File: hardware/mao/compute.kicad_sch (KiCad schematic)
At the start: 49 parts, among them J201 TAG, U201 ESP32-S3-MINI-1-N8

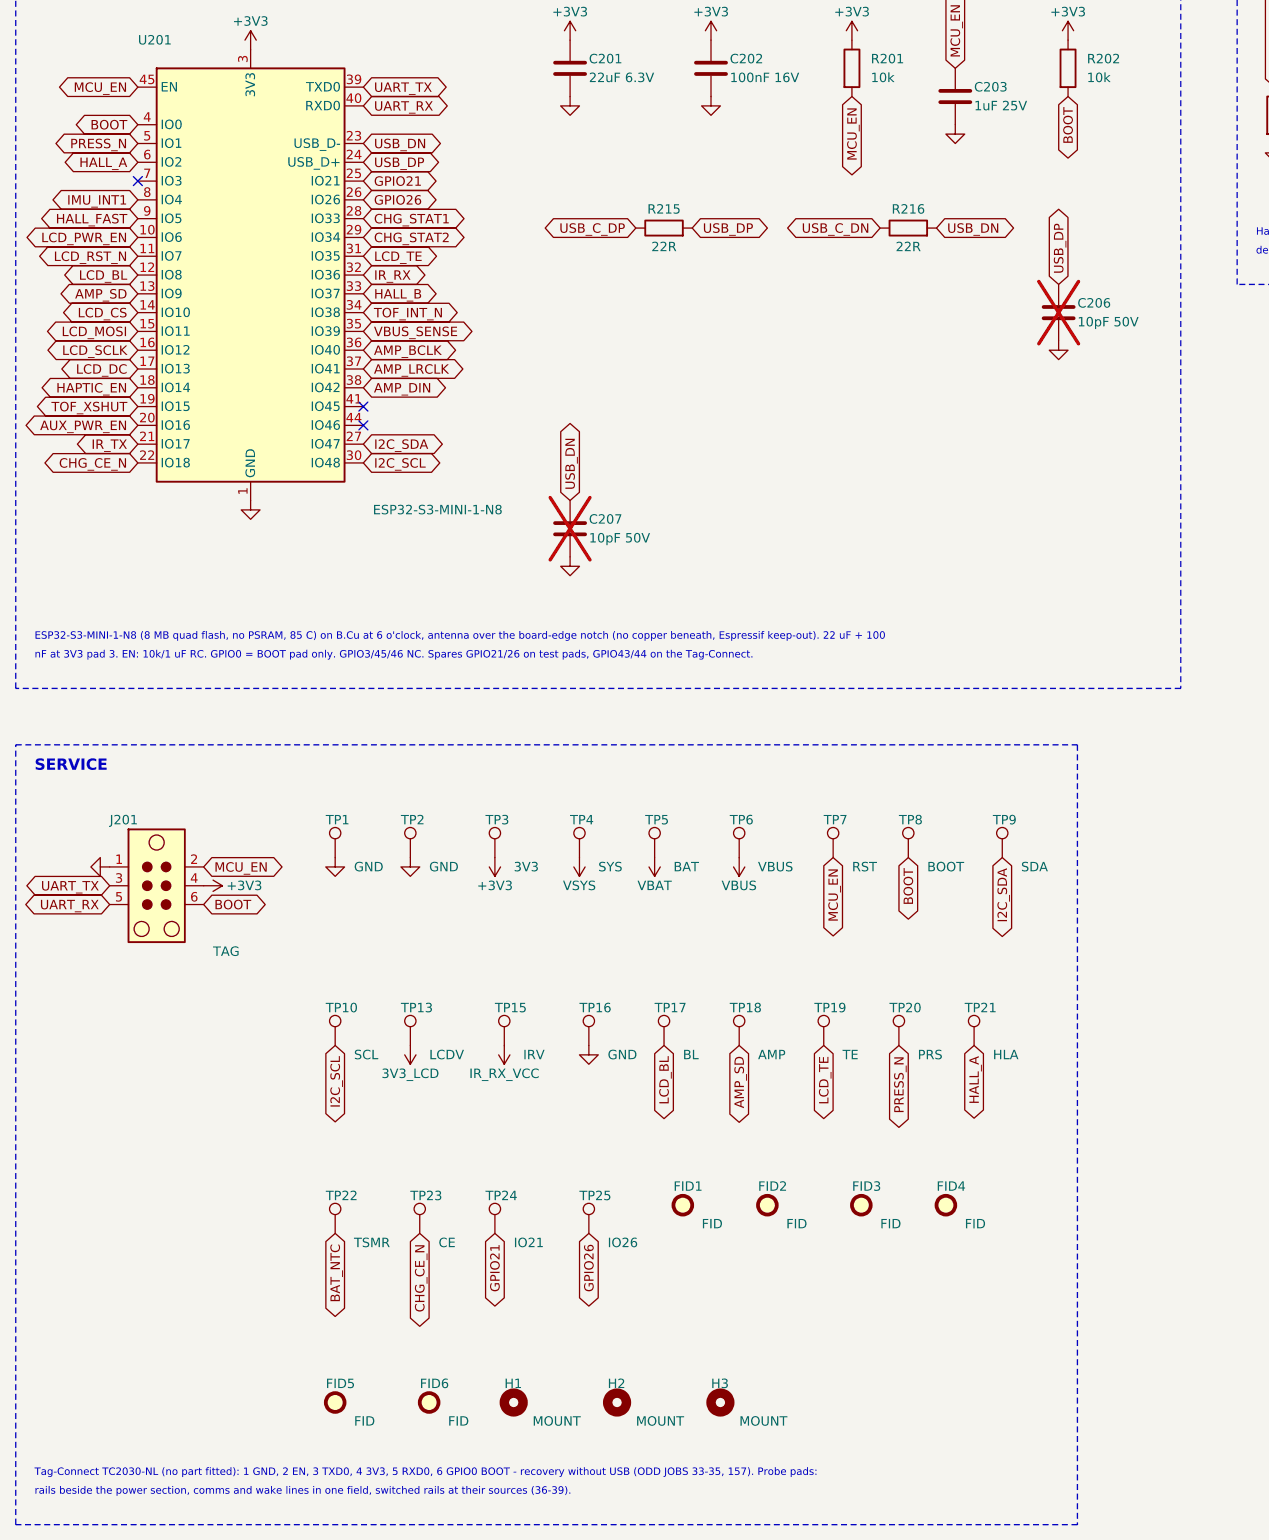
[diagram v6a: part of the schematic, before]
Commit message: A1 capture/layout follow the pin swaps (ERC 0); escapes and fixture pads moved with their nets
Co-Authored-By: Claude Opus 5.5 <noreply@anthropic.com>
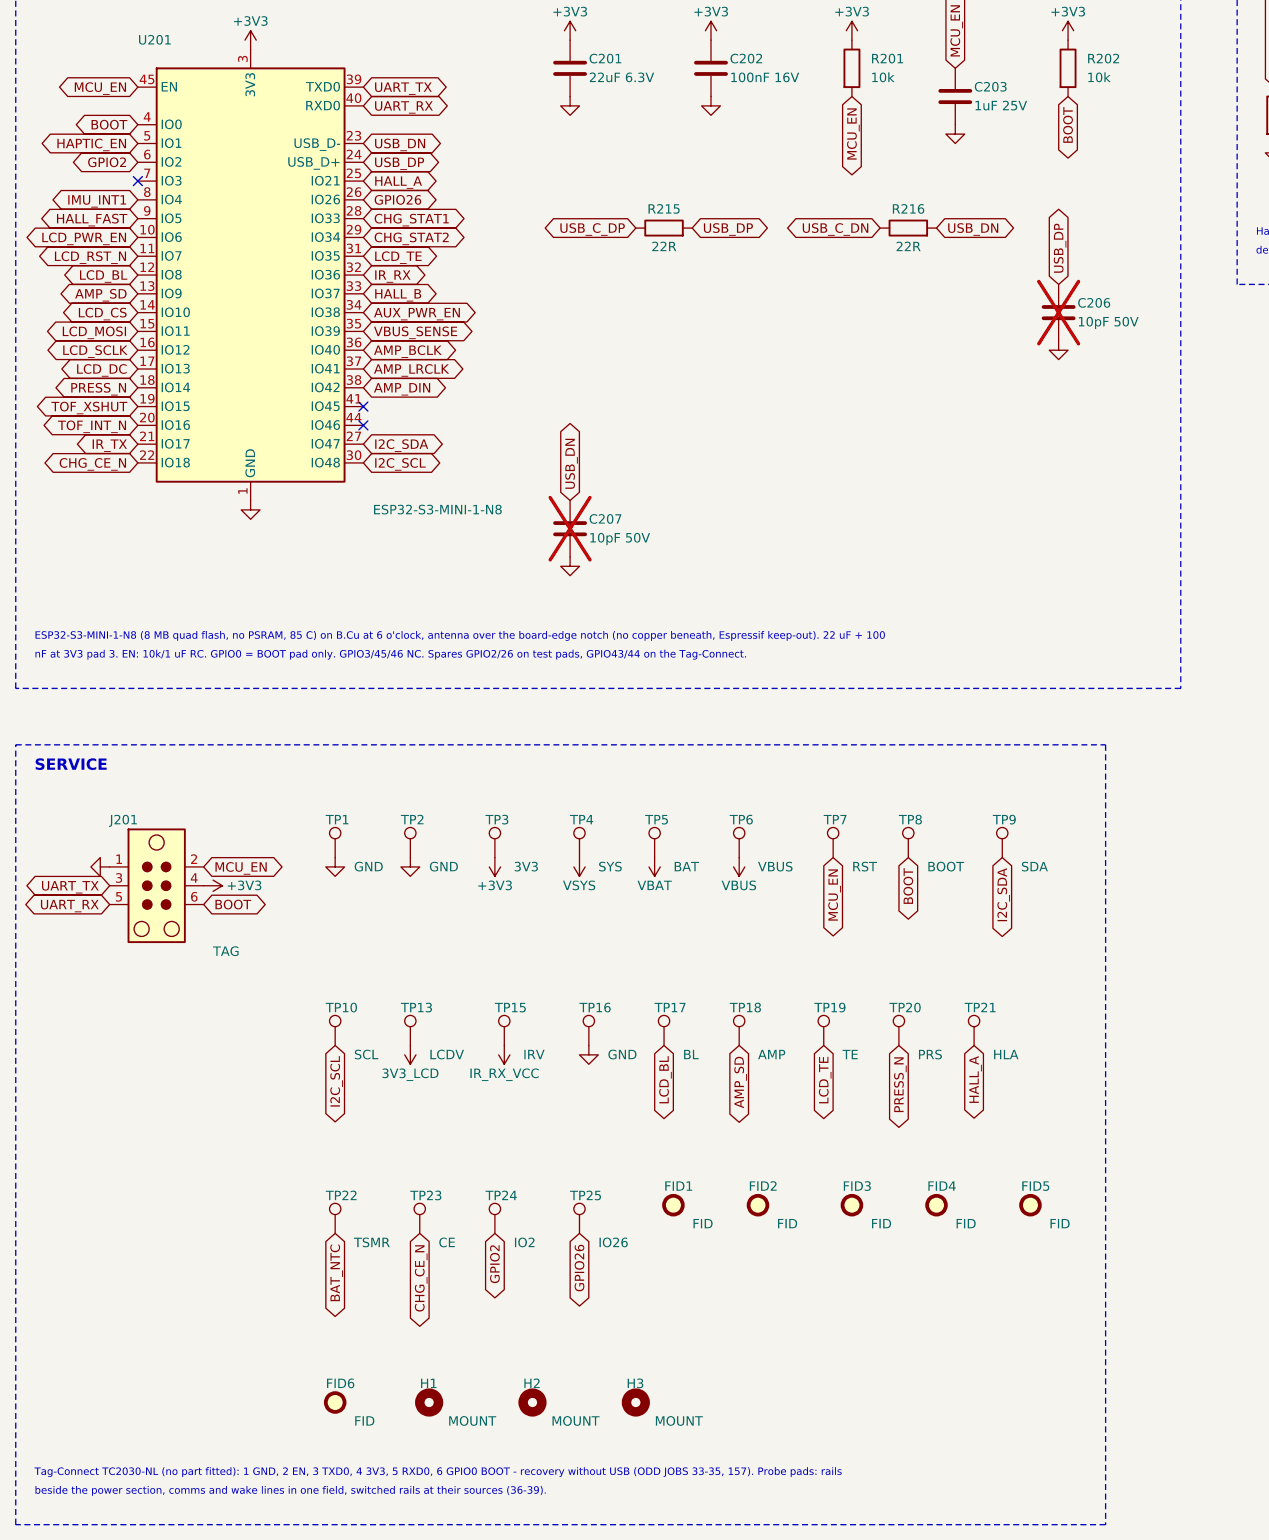
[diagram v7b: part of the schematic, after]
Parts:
- TP24: value IO21 -> IO2
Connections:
- net AUX_PWR_EN: now also U201.34 (IO38); no longer U201.20 (IO16)
- net HALL_A: now also U201.25 (IO21); no longer U201.6 (IO2)
- net HAPTIC_EN: now also U201.5 (IO1); no longer U201.18 (IO14)
- net PRESS_N: now also U201.18 (IO14); no longer U201.5 (IO1)
- net TOF_INT_N: now also U201.20 (IO16); no longer U201.34 (IO38)
- net GPIO21 renamed GPIO2
- net GPIO2: now also U201.6 (IO2); no longer U201.25 (IO21)
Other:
- note added: "Tag-Connect TC2030-NL (no part fitted): 1 GND, 2 EN, 3 TXD0, 4 3V3, 5 RXD0, 6 GPIO0 BOOT - recovery without USB (ODD JOBS 33-35, 157). Probe pads: rails"
- note added: "beside the power section, comms and wake lines in one field, switched rails at their sources (36-39)."
- note added: "nF at 3V3 pad 3. EN: 10k/1 uF RC. GPIO0 = BOOT pad only. GPIO3/45/46 NC. Spares GPIO2/26 on test pads, GPIO43/44 on the Tag-Connect."
- note removed: "Tag-Connect TC2030-NL (no part fitted): 1 GND, 2 EN, 3 TXD0, 4 3V3, 5 RXD0, 6 GPIO0 BOOT - recovery without USB (ODD JOBS 33-35, 157). Probe pads:"
- note removed: "nF at 3V3 pad 3. EN: 10k/1 uF RC. GPIO0 = BOOT pad only. GPIO3/45/46 NC. Spares GPIO21/26 on test pads, GPIO43/44 on the Tag-Connect."
- note removed: "rails beside the power section, comms and wake lines in one field, switched rails at their sources (36-39)."
- moved on the sheet: FID1, FID2, FID3, FID4, FID5, FID6, H1, H2, H3, TP25

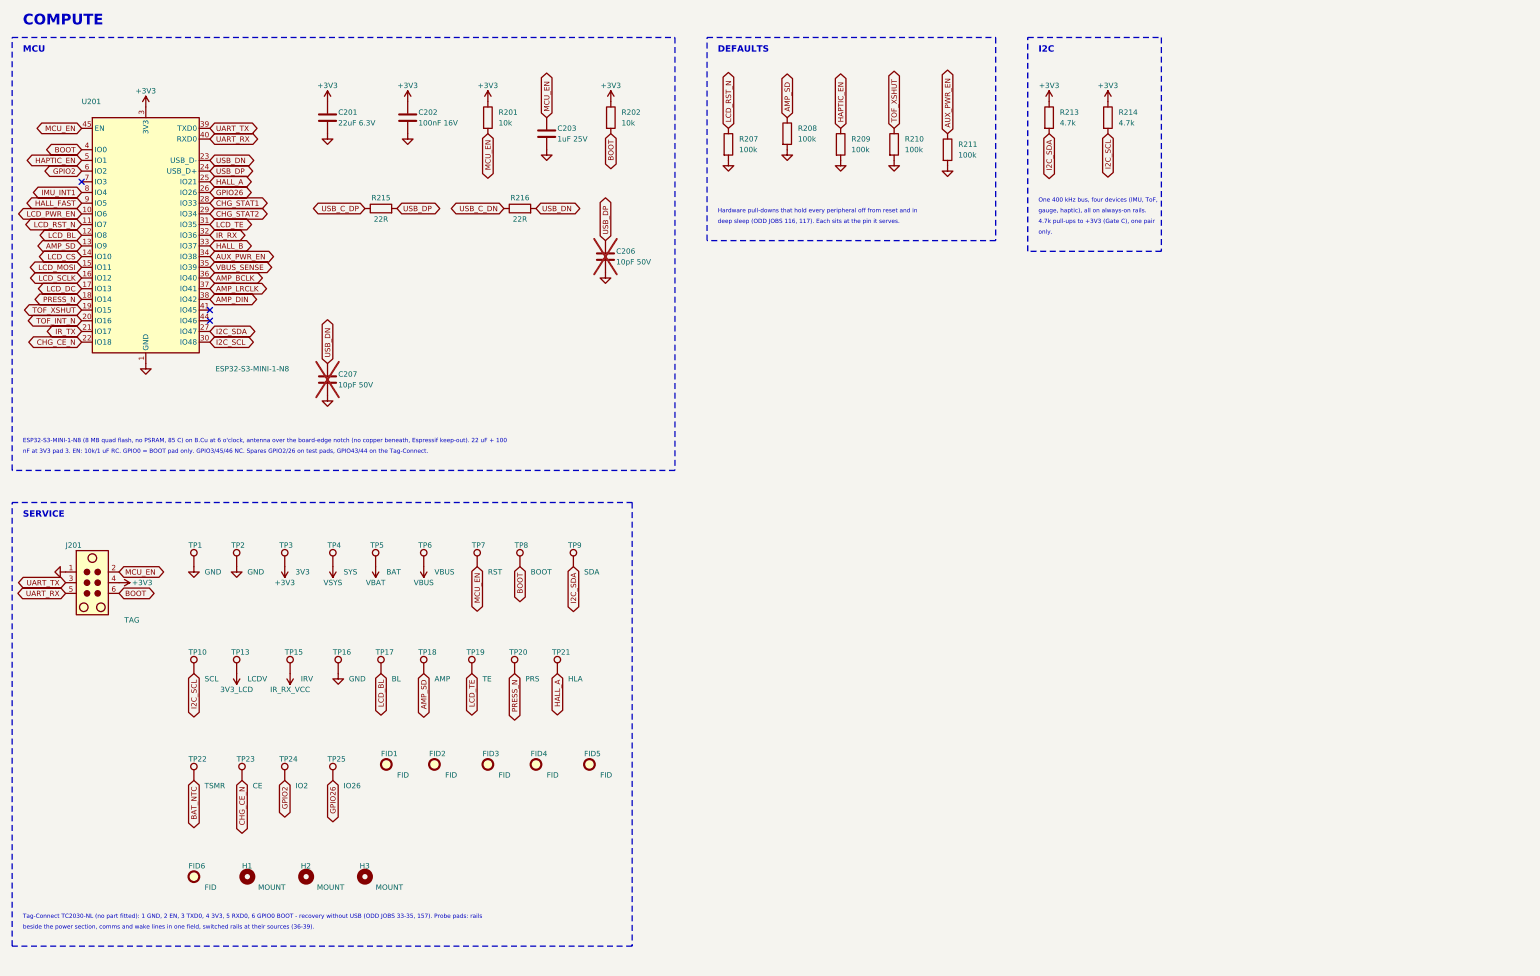
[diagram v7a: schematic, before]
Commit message: A1: USB wakes from deep sleep (design review 2026-10-06, finding 1)
VBUS_SENSE (GPIO39) is not an RTC pad. The 100k/150k VBUS divider now drives a 2N7002 (Q102, C8545 Basic) whose
drain, USB_PRESENT_N (100k pull-up R123, 33 uA only while USB is present), sits on the spare RTC pad GPIO2: an ext1
any-low wake source. GPIO39 is a spare with test pad TP26; TP24 now probes USB_PRESENT_N.

Layout (surgical, route_review.py): Q102/R123 on F east of the module's right escape column, gate on the router's
VBUS_SENSE line, drain down to an L3 run under the module (south of AMP_LRCLK) to GPIO2's stub; sync_fields.py --add
puts parts new in circuit.py on the routed board. DRC 0 / unconnected 0 / parity 0, planes continuous.

Firmware: MAO_LINE_USB_PRESENT reads GPIO2 active low, USB_PRESENT_N joins the A1 ext1 any-low mask when it idles
high (deep_sleep_hold and the critical sleep ask for it); MAO still never deep-sleeps with USB present.

Co-Authored-By: Claude Opus 5.5 <noreply@anthropic.com>
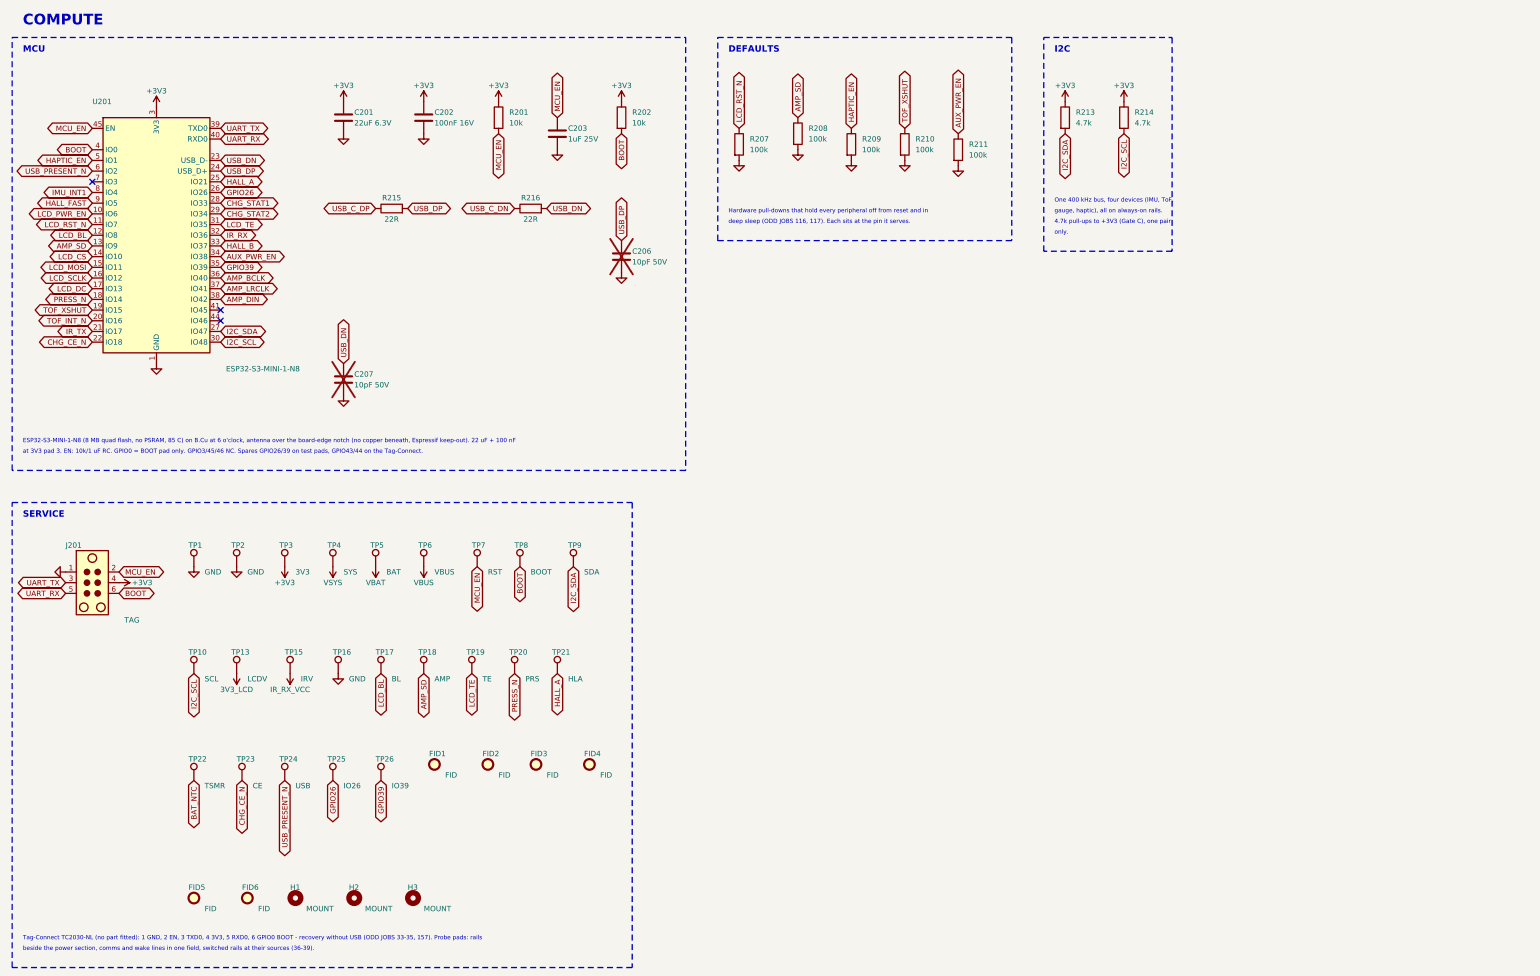
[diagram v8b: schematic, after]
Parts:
- added TP26: IO39, TestPoint:TestPoint_Pad_D1.0mm, symbol Connector:TestPoint
- TP24: value IO2 -> USB
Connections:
- net GPIO2 renamed USB_PRESENT_N
- net VBUS_SENSE renamed GPIO39
- net GPIO39: now also TP26.1
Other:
- note added: "ESP32-S3-MINI-1-N8 (8 MB quad flash, no PSRAM, 85 C) on B.Cu at 6 o'clock, antenna over the board-edge notch (no copper beneath, Espressif keep-out). 22 uF + 100 nF"
- note added: "at 3V3 pad 3. EN: 10k/1 uF RC. GPIO0 = BOOT pad only. GPIO3/45/46 NC. Spares GPIO26/39 on test pads, GPIO43/44 on the Tag-Connect."
- note removed: "ESP32-S3-MINI-1-N8 (8 MB quad flash, no PSRAM, 85 C) on B.Cu at 6 o'clock, antenna over the board-edge notch (no copper beneath, Espressif keep-out). 22 uF + 100"
- note removed: "nF at 3V3 pad 3. EN: 10k/1 uF RC. GPIO0 = BOOT pad only. GPIO3/45/46 NC. Spares GPIO2/26 on test pads, GPIO43/44 on the Tag-Connect."
- moved on the sheet: C201, C202, C203, C206, C207, FID1, FID2, FID3, FID4, FID5, FID6, H1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
